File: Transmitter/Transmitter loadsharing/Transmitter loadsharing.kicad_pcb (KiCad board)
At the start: 2 copper layers, 26.7 x 33.6 mm, 20 parts, among them J1 Conn_Coaxial, J2 Conn_01x02, J3 Conn_01x03, J4 Conn_01x02_Socket, J5 Conn_01x02, J6 Conn_01x01, U1 OPA3692IDBQR

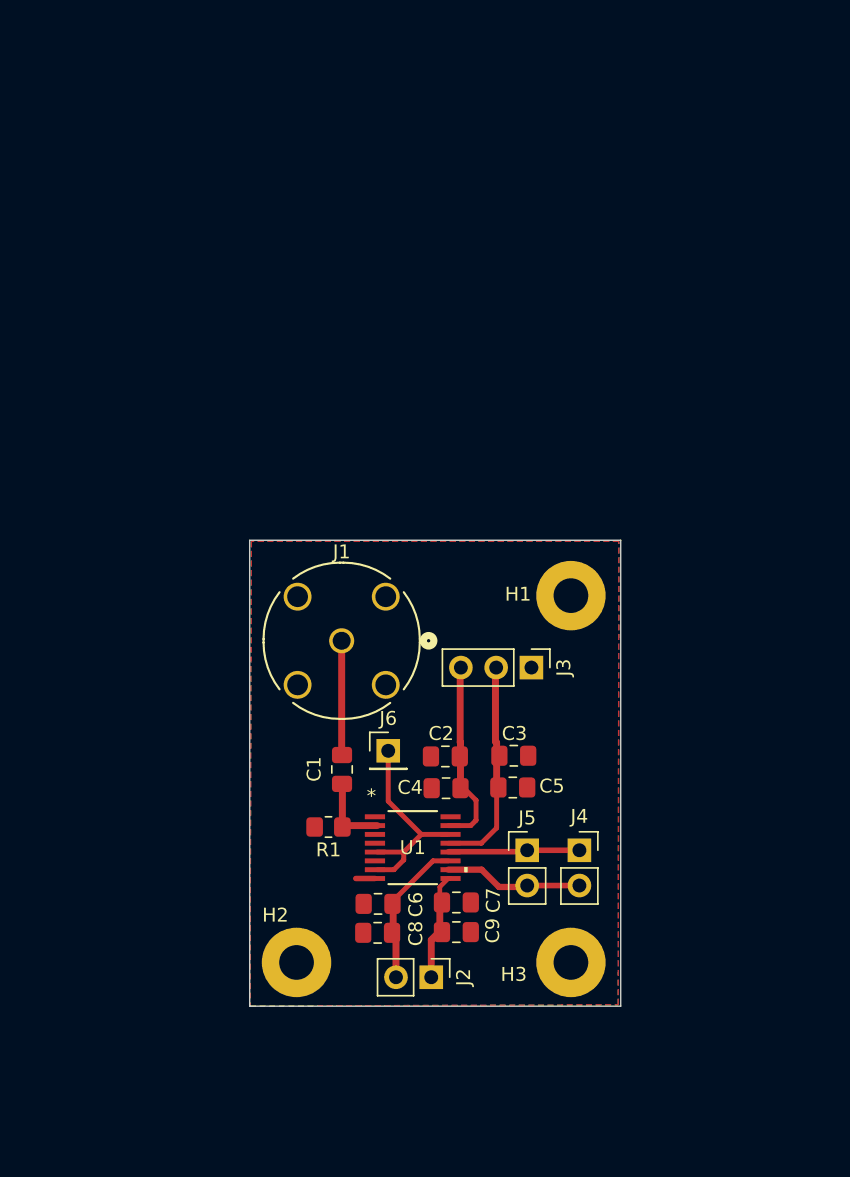
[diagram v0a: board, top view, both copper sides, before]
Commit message: mostly changes to transmitter prototype, for using the prototyper
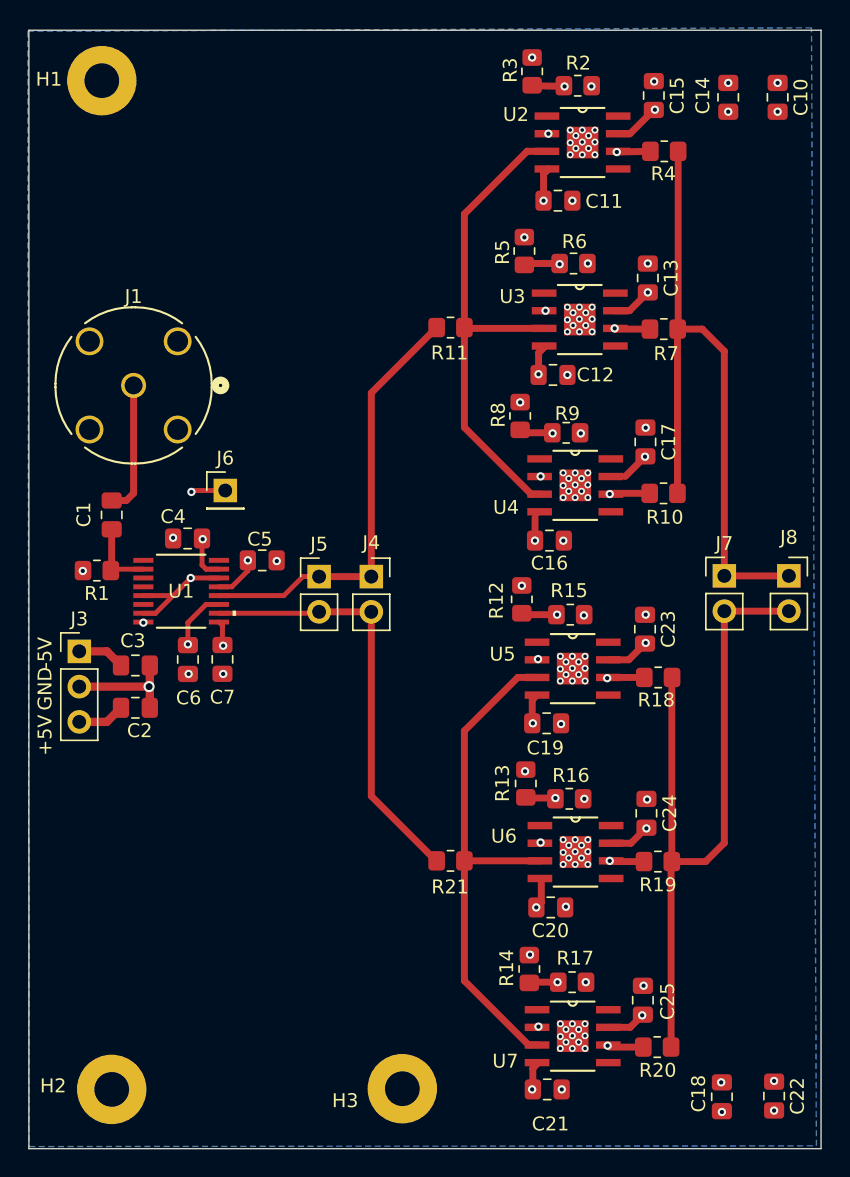
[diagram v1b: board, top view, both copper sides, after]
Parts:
- removed C8, C9: 6.8 uF, Capacitor_SMD:C_0805_2012Metric_Pad1.18x1.45mm_HandSolder
- removed J2: Conn_01x02, Connector_PinHeader_2.54mm:PinHeader_1x02_P2.54mm_Vertical
- added C10: 6.8 uF, Capacitor_SMD:C_0805_2012Metric_Pad1.18x1.45mm_HandSolder, F.Cu at (194.6, 37.7)
- added C11: 0.1 nF, Capacitor_SMD:C_0805_2012Metric_Pad1.18x1.45mm_HandSolder, F.Cu at (178.7, 45.2)
- added C12: 0.1 nF, Capacitor_SMD:C_0805_2012Metric_Pad1.18x1.45mm_HandSolder, F.Cu at (178.4, 57.7)
- added C13: 0.1 nF, Capacitor_SMD:C_0805_2012Metric_Pad1.18x1.45mm_HandSolder, F.Cu at (185.2, 50.7)
- added C14: 6.8 uF, Capacitor_SMD:C_0805_2012Metric_Pad1.18x1.45mm_HandSolder, F.Cu at (191.0, 37.7)
- added C15: 0.1 nF, Capacitor_SMD:C_0805_2012Metric_Pad1.18x1.45mm_HandSolder, F.Cu at (185.6, 37.6)
- added C16: 0.1 nF, Capacitor_SMD:C_0805_2012Metric_Pad1.18x1.45mm_HandSolder, F.Cu at (178.1, 69.6)
- added C17: 0.1 nF, Capacitor_SMD:C_0805_2012Metric_Pad1.18x1.45mm_HandSolder, F.Cu at (185.0, 62.5)
- added C18: 6.8 uF, Capacitor_SMD:C_0805_2012Metric_Pad1.18x1.45mm_HandSolder, F.Cu at (190.6, 109.7)
- added C19: 0.1 nF, Capacitor_SMD:C_0805_2012Metric_Pad1.18x1.45mm_HandSolder, F.Cu at (177.9, 82.8)
- added C20: 0.1 nF, Capacitor_SMD:C_0805_2012Metric_Pad1.18x1.45mm_HandSolder, F.Cu at (178.2, 96.1)
- added C21: 0.1 nF, Capacitor_SMD:C_0805_2012Metric_Pad1.18x1.45mm_HandSolder, F.Cu at (178.0, 109.2)
- added C22: 6.8 uF, Capacitor_SMD:C_0805_2012Metric_Pad1.18x1.45mm_HandSolder, F.Cu at (194.3, 109.6)
- added C23: 0.1 nF, Capacitor_SMD:C_0805_2012Metric_Pad1.18x1.45mm_HandSolder, F.Cu at (185.0, 76.0)
- added C24: 0.1 nF, Capacitor_SMD:C_0805_2012Metric_Pad1.18x1.45mm_HandSolder, F.Cu at (185.1, 89.3)
- added C25: 0.1 nF, Capacitor_SMD:C_0805_2012Metric_Pad1.18x1.45mm_HandSolder, F.Cu at (184.9, 102.7)
- added J7: Conn_01x02, Connector_PinHeader_2.54mm:PinHeader_1x02_P2.54mm_Vertical, F.Cu at (190.7, 72.2)
- added J8: Conn_01x02_Socket, Connector_PinSocket_2.54mm:PinSocket_1x02_P2.54mm_Vertical, F.Cu at (195.4, 72.2)
- added R10: R, Resistor_SMD:R_0805_2012Metric_Pad1.20x1.40mm_HandSolder, F.Cu at (186.4, 66.2)
- added R11: 1 Ohm, Resistor_SMD:R_0805_2012Metric_Pad1.20x1.40mm_HandSolder, F.Cu at (171.0, 54.3)
- added R12: 250 Ohm, Resistor_SMD:R_0805_2012Metric_Pad1.20x1.40mm_HandSolder, F.Cu at (176.1, 73.9)
- added R13: 250 Ohm, Resistor_SMD:R_0805_2012Metric_Pad1.20x1.40mm_HandSolder, F.Cu at (176.4, 87.1)
- added R14: 250 Ohm, Resistor_SMD:R_0805_2012Metric_Pad1.20x1.40mm_HandSolder, F.Cu at (176.7, 100.5)
- added R15: 1 kOhm, Resistor_SMD:R_0805_2012Metric_Pad1.20x1.40mm_HandSolder, F.Cu at (179.6, 75.0)
- added R16: 1 kOhm, Resistor_SMD:R_0805_2012Metric_Pad1.20x1.40mm_HandSolder, F.Cu at (179.6, 88.2)
- added R17: 1 kOhm, Resistor_SMD:R_0805_2012Metric_Pad1.20x1.40mm_HandSolder, F.Cu at (179.8, 101.4)
- added R18: R, Resistor_SMD:R_0805_2012Metric_Pad1.20x1.40mm_HandSolder, F.Cu at (186.0, 79.5)
- added R19: R, Resistor_SMD:R_0805_2012Metric_Pad1.20x1.40mm_HandSolder, F.Cu at (185.9, 92.8)
- added R2: 1 kOhm, Resistor_SMD:R_0805_2012Metric_Pad1.20x1.40mm_HandSolder, F.Cu at (180.2, 36.9)
- added R20: R, Resistor_SMD:R_0805_2012Metric_Pad1.20x1.40mm_HandSolder, F.Cu at (185.9, 106.1)
- added R21: 1 Ohm, Resistor_SMD:R_0805_2012Metric_Pad1.20x1.40mm_HandSolder, F.Cu at (171.0, 92.7)
- added R3: 250 Ohm, Resistor_SMD:R_0805_2012Metric_Pad1.20x1.40mm_HandSolder, F.Cu at (176.9, 35.9)
- added R4: R, Resistor_SMD:R_0805_2012Metric_Pad1.20x1.40mm_HandSolder, F.Cu at (186.4, 41.6)
- added R5: 250 Ohm, Resistor_SMD:R_0805_2012Metric_Pad1.20x1.40mm_HandSolder, F.Cu at (176.3, 48.8)
- added R6: 1 kOhm, Resistor_SMD:R_0805_2012Metric_Pad1.20x1.40mm_HandSolder, F.Cu at (179.9, 49.7)
- added R7: R, Resistor_SMD:R_0805_2012Metric_Pad1.20x1.40mm_HandSolder, F.Cu at (186.4, 54.4)
- added R8: 250 Ohm, Resistor_SMD:R_0805_2012Metric_Pad1.20x1.40mm_HandSolder, F.Cu at (176.0, 60.7)
- added R9: 1 kOhm, Resistor_SMD:R_0805_2012Metric_Pad1.20x1.40mm_HandSolder, F.Cu at (179.3, 61.9)
- added U2: THS3091D, THS3091DDR:DDA8_2P28X2P28, F.Cu at (180.5, 41.0)
- added U3: THS3091D, THS3091DDR:DDA8_2P28X2P28, F.Cu at (180.3, 53.7)
- added U4: THS3091D, THS3091DDR:DDA8_2P28X2P28, F.Cu at (180.0, 65.7)
- added U5: THS3091D, THS3091DDR:DDA8_2P28X2P28, F.Cu at (179.8, 78.9)
- added U6: THS3091D, THS3091DDR:DDA8_2P28X2P28, F.Cu at (180.0, 92.1)
- added U7: THS3091D, THS3091DDR:DDA8_2P28X2P28, F.Cu at (179.8, 105.3)
- moved H1 50.2 mm to (145.9, 36.5)
- moved J3 32.6 mm to (144.3, 77.6), turned to 0 degrees
- moved C3 28.0 mm to (148.3, 78.6)
- moved C4 25.9 mm to (152.1, 69.5)
- moved R1 24.9 mm to (145.5, 71.8)
- moved U1 24.9 mm to (151.6, 73.3)
- moved J4 24.8 mm to (165.3, 72.2)
- moved J5 24.8 mm to (161.5, 72.2)
- moved C1 24.7 mm to (146.6, 67.8)
- moved C5 24.4 mm to (157.5, 71.1)
- moved C7 24.3 mm to (154.6, 78.2), turned to 90 degrees
- moved J1 23.7 mm to (148.2, 58.5)
- moved C2 22.6 mm to (148.3, 81.7), turned to 180 degrees
- moved C6 22.3 mm to (152.1, 78.2), turned to 90 degrees
- moved J6 22.1 mm to (154.8, 66.0)
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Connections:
- J1 pad 3: (no net) -> GND
- J1 pad 4: (no net) -> GND
- J1 pad 5: (no net) -> GND
- J3 pad 1: GND -> -5V
- J3 pad 2: -5V -> GND
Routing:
- net /coil load end: track 0.00 -> 52.3 mm
- net /coil load start: track 0.00 -> 49.5 mm
- net /loadshare input -: track 0.00 -> 37.7 mm
- net /loadshare input +: track 0.00 -> 36.5 mm
- net /coil start: track 9.52 -> 31.4 mm
- net /coil end: track 10.1 -> 30.9 mm
- net Net-(U4-VOUT): track 0.00 -> 8.91 mm, vias 0 -> 2
- net Net-(U2-VOUT): track 0.00 -> 8.70 mm, vias 0 -> 2
- net Net-(U3-VOUT): track 0.00 -> 8.57 mm, vias 0 -> 2
- net Net-(U7-VOUT): track 0.00 -> 8.45 mm, vias 0 -> 2
- net Net-(U6-VOUT): track 0.00 -> 8.25 mm, vias 0 -> 2
- net Net-(U5-VOUT): track 0.00 -> 8.22 mm, vias 0 -> 2
- net GND: track 1.38 -> 8.12 mm, vias 0 -> 107
- net Net-(U5-VIN-): track 0.00 -> 6.69 mm, vias 0 -> 2
- net Net-(U3-VIN-): track 0.00 -> 6.65 mm, vias 0 -> 2
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- added copper zone on In2.Cu, net +5V
- added copper zone on B.Cu, net -5V
- added copper zone on In1.Cu, net GND
- removed copper zone on B.Cu, net GND
- removed copper zone on F.Cu, net GND
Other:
- board size 26.7 x 33.6 mm -> 57 x 80.5 mm
- copper layers 2 -> 4
- board text added: "+5V"
- board text added: "-5V"
- board text added: "GND"

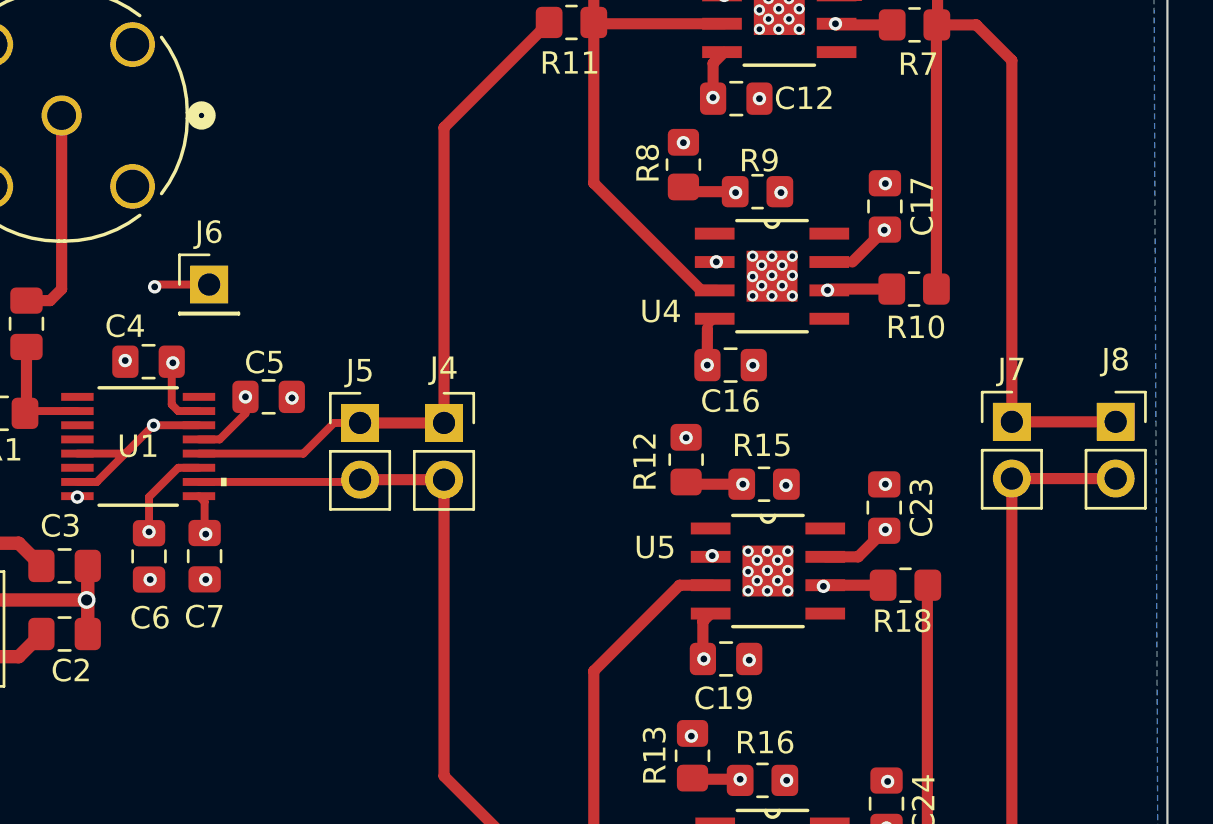
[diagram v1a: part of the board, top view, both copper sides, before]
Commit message: added footprints for SOIC and SSOP for OPA3692
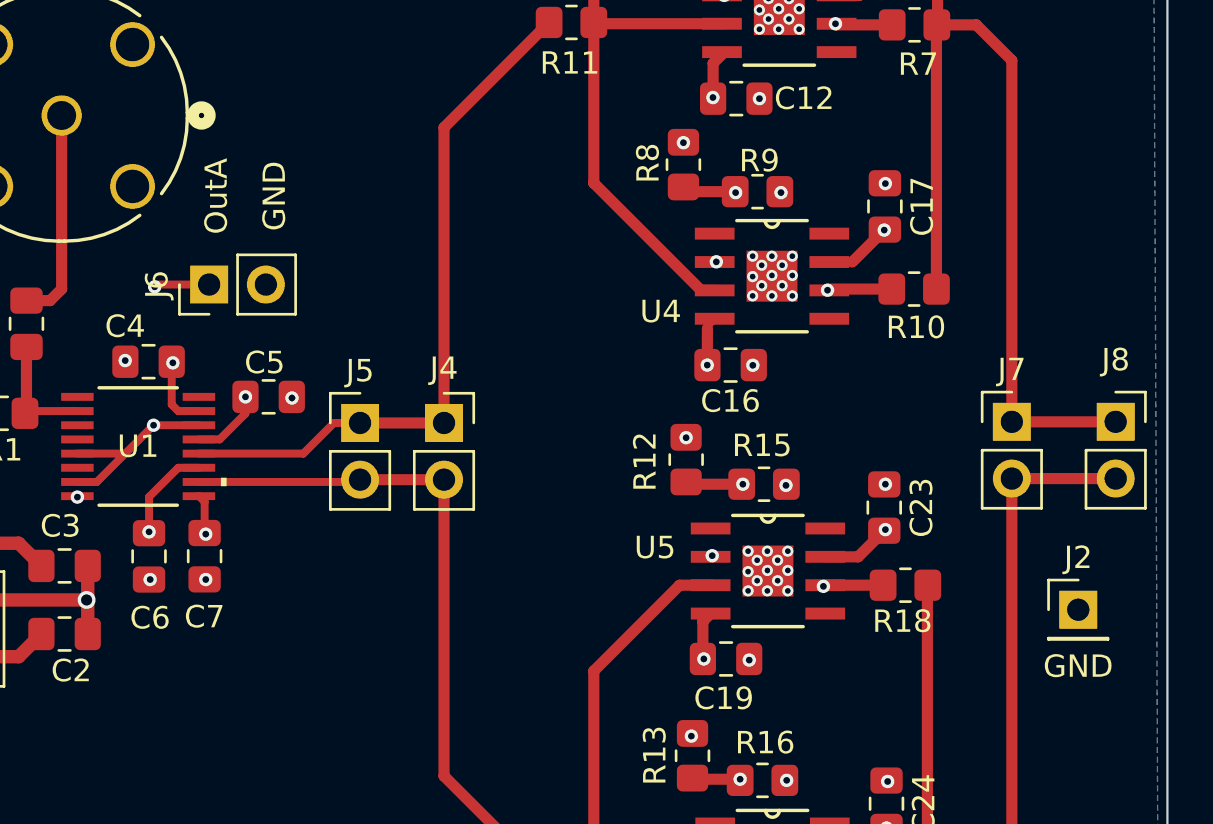
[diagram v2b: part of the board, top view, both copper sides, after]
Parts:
- added J2: Conn_01x01, Connector_PinHeader_2.54mm:PinHeader_1x01_P2.54mm_Vertical, F.Cu at (193.7, 80.6)
- J6: value Conn_01x01 -> Conn_01x02; footprint Connector_PinHeader_2.54mm:PinHeader_1x01_P2.54mm_Vertical -> Connector_PinHeader_2.54mm:PinHeader_1x02_P2.54mm_Vertical
- turned J6 to 90 degrees
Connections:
- J1 pad 3: GND -> (no net)
- J1 pad 4: GND -> (no net)
- J1 pad 5: GND -> (no net)
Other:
- board text added: "OutA"

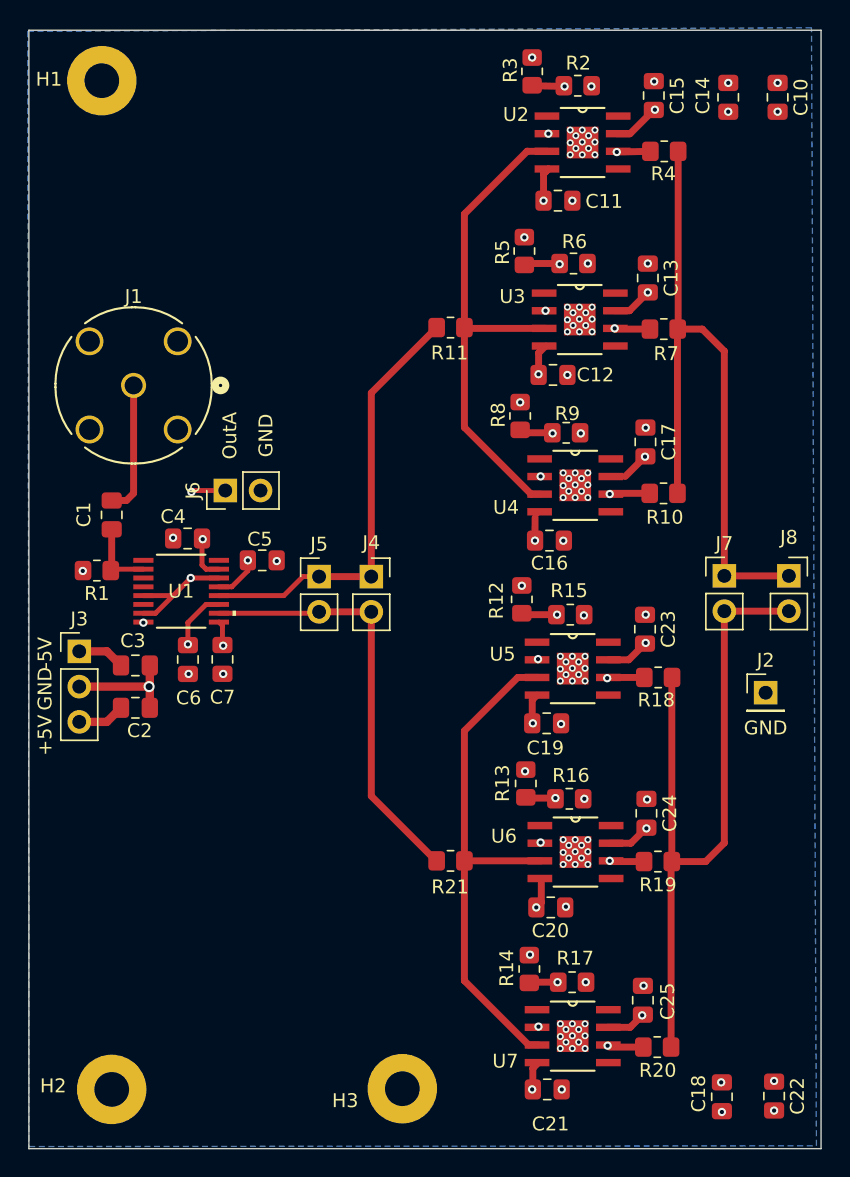
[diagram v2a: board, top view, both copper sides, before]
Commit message: added 3d models for OPA3692, THS3091 and BNC connector
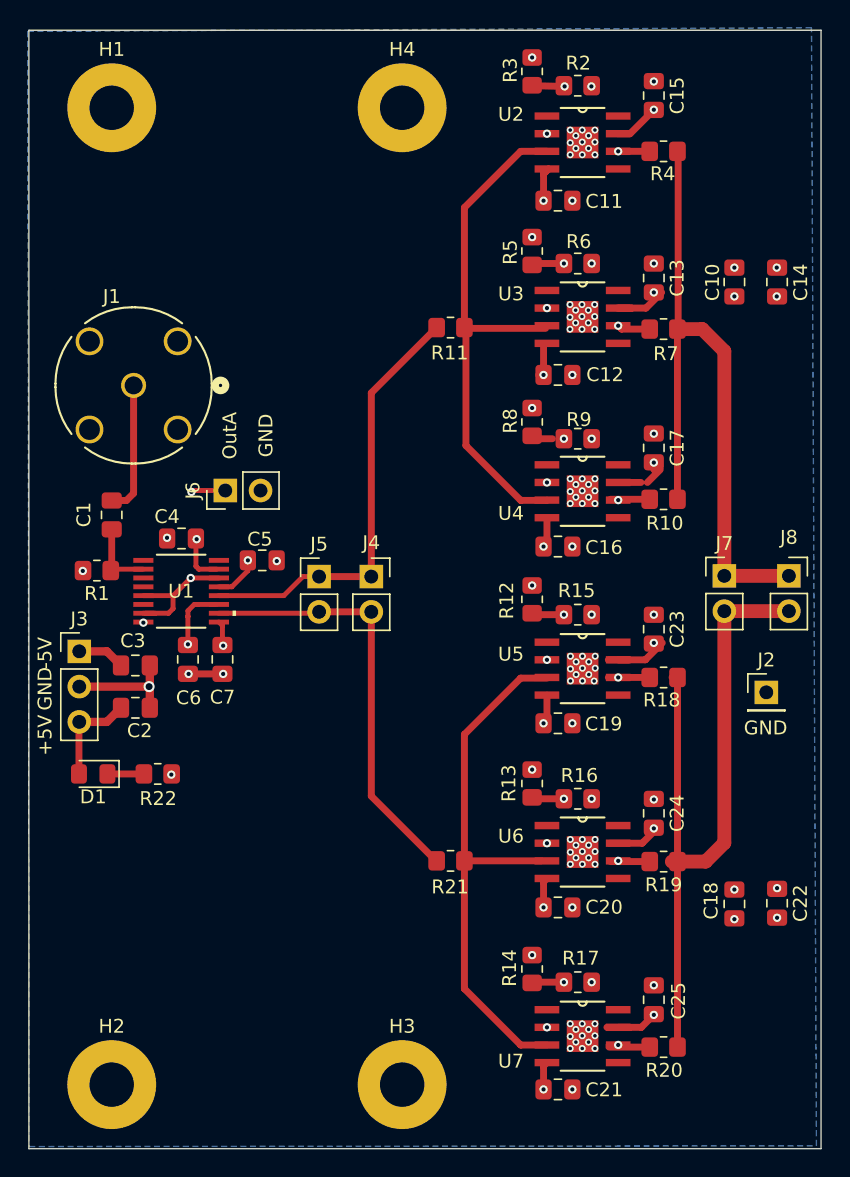
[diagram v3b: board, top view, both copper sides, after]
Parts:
- added D1: LED, LED_SMD:LED_0805_2012Metric_Pad1.15x1.40mm_HandSolder, F.Cu at (145.3, 86.5)
- added H4: MountingHole, MountingHole:MountingHole_3.2mm_M3_Pad, F.Cu at (167.5, 38.5)
- added R22: R, Resistor_SMD:R_0805_2012Metric_Pad1.20x1.40mm_HandSolder, F.Cu at (149.9, 86.5)
- H1, H2, H3: footprint MountingHole:MountingHole_2.5mm_Pad -> MountingHole:MountingHole_3.2mm_M3_Pad
- moved C18 13.9 mm to (191.4, 95.8)
- moved C22 13.9 mm to (194.5, 95.8)
- moved C14 13.8 mm to (194.5, 51.0)
- moved C10 13.7 mm to (191.4, 51.0)
- moved H1 2.08 mm to (146.6, 38.5)
- moved R8 0.96 mm to (176.9, 61.1)
- moved R9 0.94 mm to (180.2, 62.3)
- moved C19 0.81 mm to (178.7, 82.8)
- moved C25 0.79 mm to (185.6, 102.7)
- moved C21 0.77 mm to (178.7, 109.2)
- moved C16 0.74 mm to (178.7, 70.1)
- moved R12 0.74 mm to (176.9, 73.9)
- moved C17 0.74 mm to (185.6, 63.0)
- moved U5 0.71 mm to (180.5, 78.9)
- moved U7 0.71 mm to (180.5, 105.3)
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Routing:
- net +5V: track 30.0 -> 41.4 mm
- net Net-(D1-K): track 0.00 -> 2.62 mm
- net GND: track 8.12 -> 10.6 mm, vias 107 -> 108
- net Net-(J6-Pin_1): track 17.7 -> 19.2 mm
- net /loadshare input +: track 36.5 -> 37.9 mm
- net /loadshare input -: track 37.7 -> 39.1 mm
- net Net-(U4-VOUT): track 8.91 -> 9.87 mm
- net /coil load end: track 52.3 -> 53.2 mm
- net Net-(U5-VIN-): track 6.69 -> 5.84 mm
- net Net-(U3-VIN-): track 6.65 -> 6.01 mm
- net Net-(U4-VIN-): track 6.04 -> 5.53 mm
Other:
- board text added: "Transmitter 1.0 2024-04-19"
